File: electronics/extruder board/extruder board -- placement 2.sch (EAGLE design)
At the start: 22 parts, among them IC1 MAX6675, IC2 MAX6675, J1 Main THERMO, J2 AUX THERMO, J3 Main Heater, J4 Secondary HEATER, X1 22-23-2041, X2 Right Fan, X3 Left Fan, X4 Extruder Fan

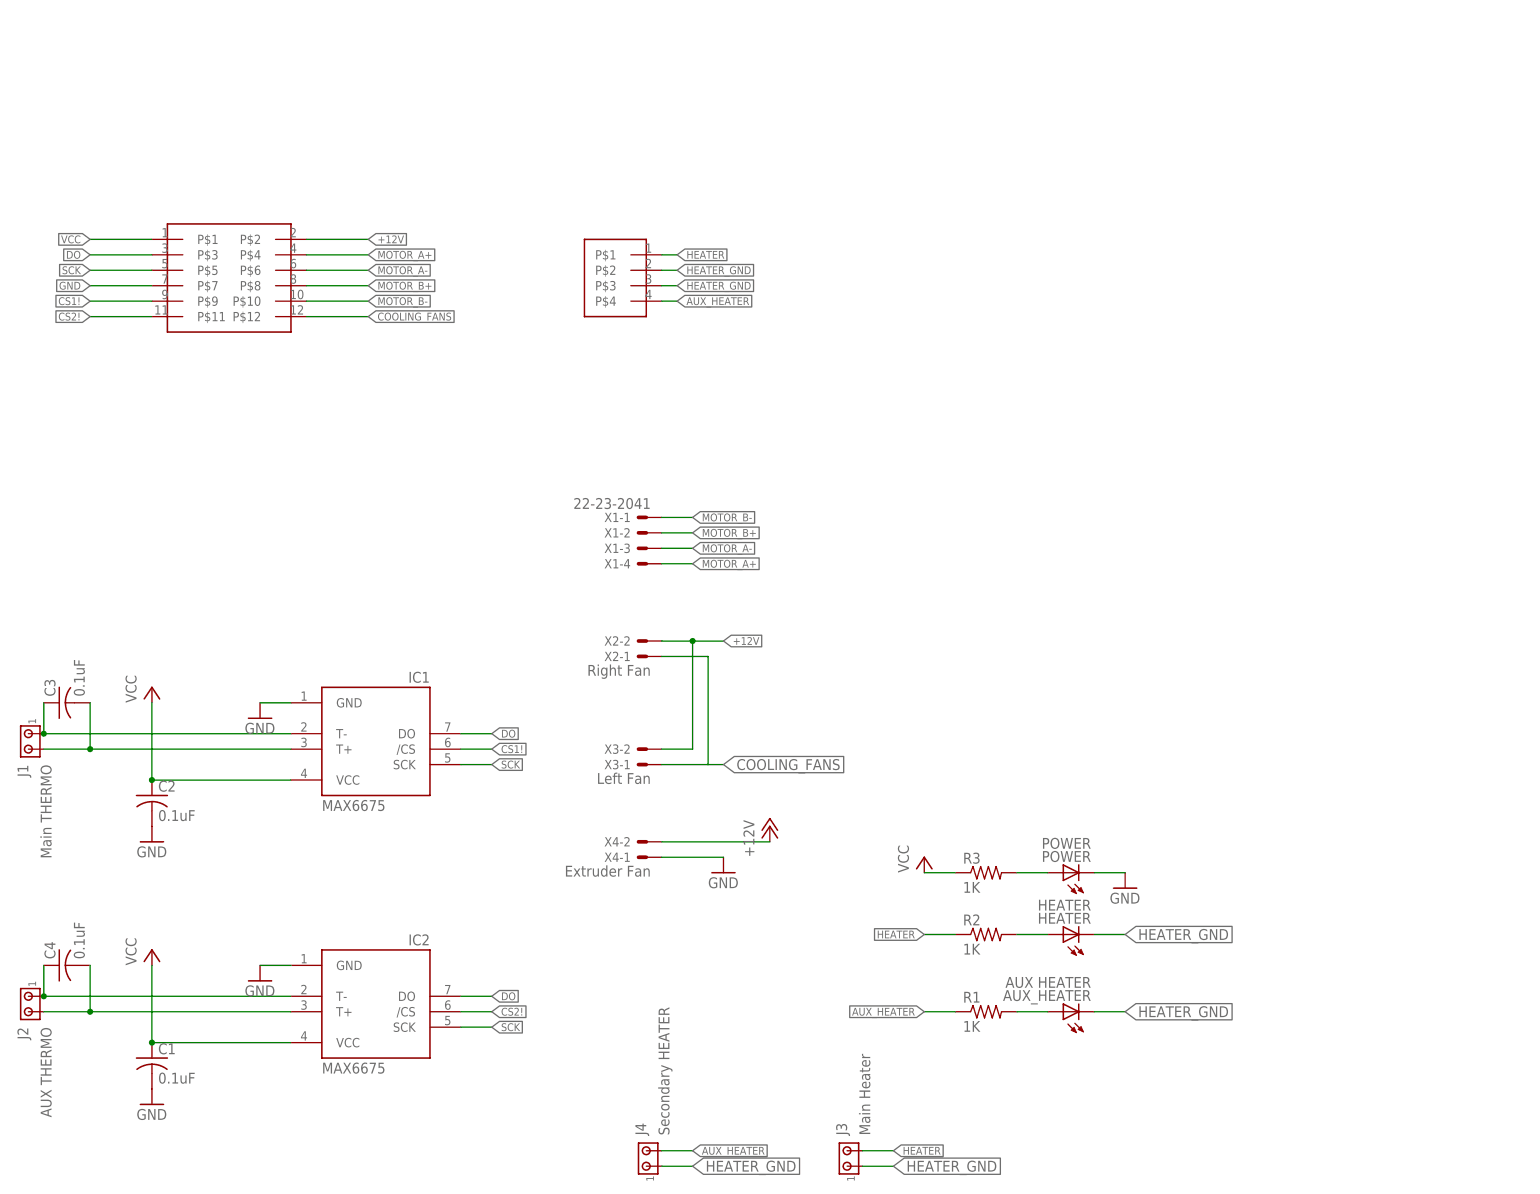
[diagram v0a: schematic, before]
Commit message: Extruder board V1.2
-Changed harness pin assignment
-Added nozzle fan driver and using pin CS1 as control signal
-Added invert circuit and using pin CS2 to control both thermocouple ADC
-Isolated the AUX heater GND and Heater GND
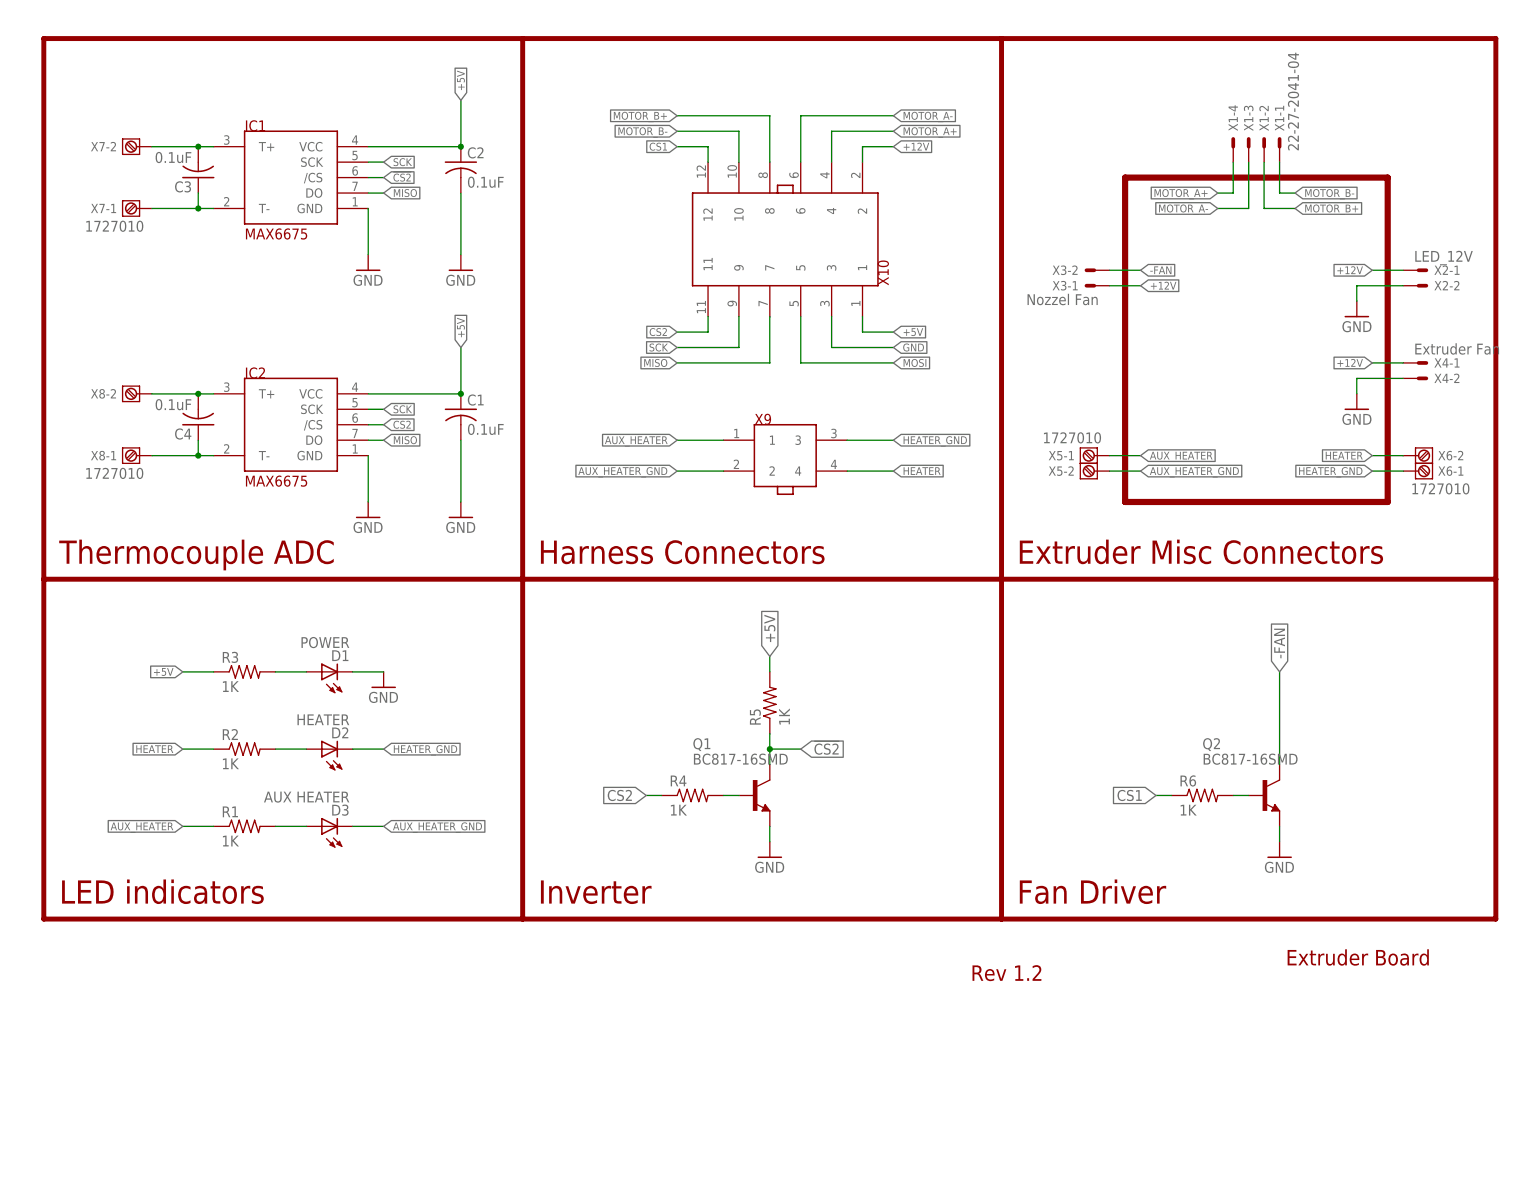
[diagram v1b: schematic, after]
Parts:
- removed AUX_HEATER: AUX HEATER, led:LEDCHIP-LED0805
- removed HEATER: HEATER, led:LEDCHIP-LED0805
- removed J1: Main THERMO, 555 delay toggle switch:CON-AMP_MTA02-156
- removed J2: AUX THERMO, 555 delay toggle switch:CON-AMP_MTA02-156
- removed J3: Main Heater, 555 delay toggle switch:CON-AMP_MTA02-156
- removed J4: Secondary HEATER, 555 delay toggle switch:CON-AMP_MTA02-156
- removed POWER: POWER, led:LEDCHIP-LED0805
- removed U$1: MOLEX_5557_6X2, extruder lib:MOLEX_5557_6X2
- removed U$3: MOLEX_5557_2X2, extruder board -- placement 2:MOLEX_5557_2X2
- added D1: POWER, extruder_board_--_placement_2:LEDCHIPLED_0805
- added D2: HEATER, extruder_board_--_placement_2:LEDCHIPLED_0805
- added D3: AUX HEATER, extruder_board_--_placement_2:LEDCHIPLED_0805
- added Q1, Q2: BC817-16SMD, extruder_board_--_placement_2:BC817-16SMD
- added R4, R5, R6: 1K, extruder_board_--_placement_2:R-US_R0603
- added X10: 5557-12, extruder_board_--_placement_2:5557-12
- added X5, X6, X7, X8: 1727010, extruder_board_--_placement_2:1727010
- added X9: 5557-04, extruder_board_--_placement_2:5557-04
- C1, C2, C3, C4: device rcl:C-USC0603 -> extruder_board_--_placement_2:C-USC0603K
- IC1, IC2: device adafruit:MAX6675 -> extruder_board_--_placement_2:MAX6675
- R1, R2, R3: device rcl:R-US_R0603 -> extruder_board_--_placement_2:R-US_R0603
- X1: value 22-23-2041 -> 22-27-2041-04; device con-molex:22-23-2041 -> extruder_board_--_placement_2:22-27-2041-04; OC_FARNELL (none) -> unknown; OC_NEWARK (none) -> unknown
- X2: value Right Fan -> LED_12V; device con-molex:22-23-2021 -> extruder_board_--_placement_2:22-27-2021-02; OC_FARNELL (none) -> unknown; OC_NEWARK (none) -> unknown
- X3: value Left Fan -> Nozzel Fan; device con-molex:22-23-2021 -> extruder_board_--_placement_2:22-27-2021-02; OC_FARNELL (none) -> unknown; OC_NEWARK (none) -> unknown
- X4: device con-molex:22-23-2021 -> extruder_board_--_placement_2:22-27-2021-02; MF MOLEX -> (none); MPN 22-23-2021 -> (none); OC_FARNELL 1462926 -> unknown; OC_NEWARK 25C3832 -> unknown
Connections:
- removed net COOLING_FANS: U$1.P$12, X2-1.S, X3-1.S
- removed net CS1!: IC1./CS, U$1.P$9
- removed net CS2!: IC2./CS, U$1.P$11
- removed net DO: IC1.DO, IC2.DO, U$1.P$3
- removed net VCC: C1.1, C2.1, IC1.VCC, IC2.VCC, R3.1, U$1.P$1
- new net !CS2: IC1./CS, Q1.C, R5.1
- new net +5V: C1.1, C2.1, IC1.VCC, IC2.VCC, R3.1, R5.2, X10.1
- new net -FAN: Q2.C, X3-2.S
- new net AUX_HEATER_GND: D3.C, X5-2.1, X9.2
- new net CS1: R6.1, X10.12
- new net CS2: IC2./CS, R4.1, X10.11
- new net MISO: IC1.DO, IC2.DO, X10.7
- new net MOSI: X10.5
- new net N$6: Q1.B, R4.2
- new net N$9: Q2.B, R6.2
- net +12V: now also X10.2, X2-1.S, X3-1.S, X4-1.S; no longer U$1.P$2, X2-2.S, X3-2.S, X4-2.S
- net AUX_HEATER: now also X5-1.1, X9.1; no longer J4.2, U$3.P$4
- net GND: now also D1.C, Q1.E, Q2.E, X10.3, X2-2.S, X4-2.S; no longer POWER.C, U$1.P$7, X4-1.S
- net HEATER: now also X6-2.1, X9.4; no longer J3.2, U$3.P$1
- net HEATER_GND: now also D2.C, X6-1.1, X9.3; no longer AUX_HEATER.C, HEATER.C, J3.1, J4.1, U$3.P$2, U$3.P$3
- net MOTOR_A+: now also X10.4; no longer U$1.P$4
- net MOTOR_A-: now also X10.6; no longer U$1.P$6
- net MOTOR_B+: now also X10.8; no longer U$1.P$8
- net MOTOR_B-: now also X10.10; no longer U$1.P$10
- net N$1: now also X8-1.1; no longer J2.1
- net N$2: now also X7-1.1; no longer J1.1
- net N$3: now also X7-2.1; no longer J1.2
- net N$4: now also X8-2.1; no longer J2.2
- net N$5: now also D1.A; no longer POWER.A
- net N$7: now also D2.A; no longer HEATER.A
- net N$8: now also D3.A; no longer AUX_HEATER.A
- net SCK: now also X10.9; no longer U$1.P$5
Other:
- note added: "Extruder Board"
- note added: "Extruder Misc Connectors"
- note added: "Fan Driver"
- note added: "Harness Connectors"
- note added: "Inverter"
- note added: "LED indicators"
- note added: "Rev 1.2"
- note added: "Thermocouple ADC"
- moved on the sheet: C1, C2, C3, C4, IC1, IC2, R1, R2, R3, X1-1, X1-2, X1-3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

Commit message: Extruder board V1.3
1. remove the T style cutouts in the front
2. Added holes for filament insert
3. extended board size
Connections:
- net AUX_HEATER: now also R2.1, X6-2.1, X9.4; no longer R1.1, X5-1.1, X9.1
- net AUX_HEATER_GND: now also D2.C, X6-1.1, X9.3; no longer D3.C, X5-2.1, X9.2
- net HEATER: now also R1.1, X5-1.1, X9.1; no longer R2.1, X6-2.1, X9.4
- net HEATER_GND: now also D3.C, X5-2.1, X9.2; no longer D2.C, X6-1.1, X9.3
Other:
- note added: "Rev 1.3"
- note removed: "Rev 1.2"
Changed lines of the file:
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@@
 <text x="172.72" y="30.48" size="3.81" layer="94">Fan Driver</text>
 <text x="216.916" y="20.32" size="2.54" layer="94">Extruder Board</text>
-<text x="165.1" y="17.78" size="2.54" layer="94">Rev 1.2</text>
+<text x="165.1" y="17.78" size="2.54" layer="94">Rev 1.3</text>
 </plain>
 <instances>
@@
 </segment>
 </net>
-<net name="HEATER" class="0">
+<net name="AUX_HEATER" class="0">
 <segment>
 <wire x1="236.22" y1="104.14" x2="231.14" y2="104.14" width="0.1524" layer="91"/>
@@
 <pinref part="R2" gate="G$1" pin="1"/>
 <label x="35.56" y="55.88" size="1.27" layer="95" rot="R180" xref="yes"/>
-</segment>
-</net>
-<net name="AUX_HEATER" class="0">
-<segment>
-<wire x1="187.96" y1="104.14" x2="193.04" y2="104.14" width="0.1524" layer="91"/>
-<label x="193.04" y="104.14" size="1.27" layer="95" xref="yes"/>
-<pinref part="X5" gate="-1" pin="1"/>
-</segment>
-<segment>
-<wire x1="124.46" y1="106.68" x2="116.84" y2="106.68" width="0.1524" layer="91"/>
-<label x="116.84" y="106.68" size="1.27" layer="95" rot="R180" xref="yes"/>
-<pinref part="X9" gate="G$1" pin="1"/>
-</segment>
-<segment>
-<wire x1="35.56" y1="43.18" x2="40.64" y2="43.18" width="0.1524" layer="91"/>
-<pinref part="R1" gate="G$1" pin="1"/>
-<label x="35.56" y="43.18" size="1.27" layer="95" rot="R180" xref="yes"/>
 </segment>
 </net>
@@
 </segment>
 </net>
-<net name="HEATER_GND" class="0">
+<net name="AUX_HEATER_GND" class="0">
 <segment>
 <wire x1="144.78" y1="106.68" x2="152.4" y2="106.68" width="0.1524" layer="91"/>
@@
 </segment>
 </net>
-<net name="AUX_HEATER_GND" class="0">
+<net name="HEATER_GND" class="0">
 <segment>
 <wire x1="124.46" y1="101.6" x2="116.84" y2="101.6" width="0.1524" layer="91"/>
@@
 </segment>
 </net>
+<net name="HEATER" class="0">
+<segment>
+<wire x1="124.46" y1="106.68" x2="116.84" y2="106.68" width="0.1524" layer="91"/>
+<label x="116.84" y="106.68" size="1.27" layer="95" rot="R180" xref="yes"/>
+<pinref part="X9" gate="G$1" pin="1"/>
+</segment>
+<segment>
+<wire x1="187.96" y1="104.14" x2="193.04" y2="104.14" width="0.1524" layer="91"/>
+<label x="193.04" y="104.14" size="1.27" layer="95" xref="yes"/>
+<pinref part="X5" gate="-1" pin="1"/>
+</segment>
+<segment>
+<wire x1="35.56" y1="43.18" x2="40.64" y2="43.18" width="0.1524" layer="91"/>
+<pinref part="R1" gate="G$1" pin="1"/>
+<label x="35.56" y="43.18" size="1.27" layer="95" rot="R180" xref="yes"/>
+</segment>
+</net>
